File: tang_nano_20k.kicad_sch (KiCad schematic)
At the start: 11 parts, among them J3 Conn_Coaxial, J4 Conn_Coaxial, J5 Conn_01x02_Pin, J6 Conn_01x02_Pin, J7 Conn_01x04_Pin, U2 Tang_Nano_20K, U5 Adafruit_PCM510x

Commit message: Added information about DIN/RCA connectors
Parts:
- J5: footprint (none) -> Connector_PinHeader_2.54mm:PinHeader_1x02_P2.54mm_Vertical
- J6: footprint (none) -> Connector_PinHeader_2.54mm:PinHeader_1x02_P2.54mm_Vertical_SMD_Pin1Left
- J7: footprint (none) -> Connector_PinHeader_2.54mm:PinHeader_1x04_P2.54mm_Vertical
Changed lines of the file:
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@@
 			)
 		)
-		(property "Footprint" ""
+		(property "Footprint" "Connector_PinHeader_2.54mm:PinHeader_1x02_P2.54mm_Vertical_SMD_Pin1Left"
 			(at 210.82 101.6 0)
 			(hide yes)
@@
 			)
 		)
-		(property "Footprint" ""
+		(property "Footprint" "Connector_PinHeader_2.54mm:PinHeader_1x04_P2.54mm_Vertical"
 			(at 210.82 77.47 0)
 			(hide yes)
@@
 			)
 		)
-		(property "Datasheet" ""
+		(property "Datasheet" "https://www.kycon.com/Catalog_PDF/KLPX.pdf"
 			(at 68.58 115.57 0)
 			(hide yes)
@@
 			)
 		)
-		(property "Description" "coaxial connector (BNC, SMA, SMB, SMC, Cinch/RCA, LEMO, ...)"
+		(property "Description" "Kycon KLPX-0848A RCA card-edge female RCA connector"
 			(at 68.58 115.57 0)
 			(hide yes)
@@
 			)
 		)
-		(property "Footprint" ""
+		(property "Footprint" "Connector_PinHeader_2.54mm:PinHeader_1x02_P2.54mm_Vertical"
 			(at 210.82 91.44 0)
 			(hide yes)
@@
 			)
 		)
-		(property "Datasheet" ""
+		(property "Datasheet" "https://www.kycon.com/Catalog_PDF/KLPX.pdf"
 			(at 220.98 128.27 0)
 			(hide yes)
@@
 			)
 		)
-		(property "Description" "coaxial connector (BNC, SMA, SMB, SMC, Cinch/RCA, LEMO, ...)"
+		(property "Description" "Kycon KLPX-0848A RCA card-edge female RCA connector"
 			(at 220.98 128.27 0)
 			(hide yes)

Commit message: New official footprints for DIN/RCA
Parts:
- J3, J4: footprint (none) -> noaidi-fpga-synth:RCA_Kycon_KLPX-0848A
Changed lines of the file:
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@@
 			)
 		)
-		(property "Footprint" ""
+		(property "Footprint" "noaidi-fpga-synth:RCA_Kycon_KLPX-0848A"
 			(at 68.58 115.57 0)
 			(hide yes)
@@
 			)
 		)
-		(property "Footprint" ""
+		(property "Footprint" "noaidi-fpga-synth:RCA_Kycon_KLPX-0848A"
 			(at 220.98 128.27 0)
 			(hide yes)

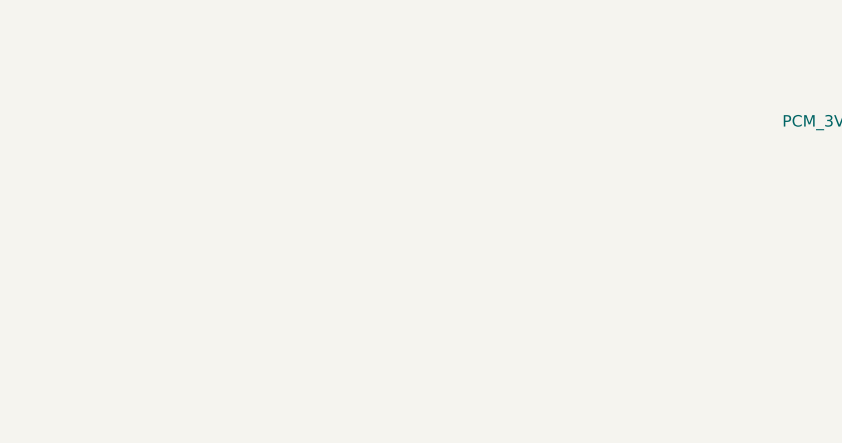
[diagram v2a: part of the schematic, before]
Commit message: Added LM66100 ideal diodes for power source switching.
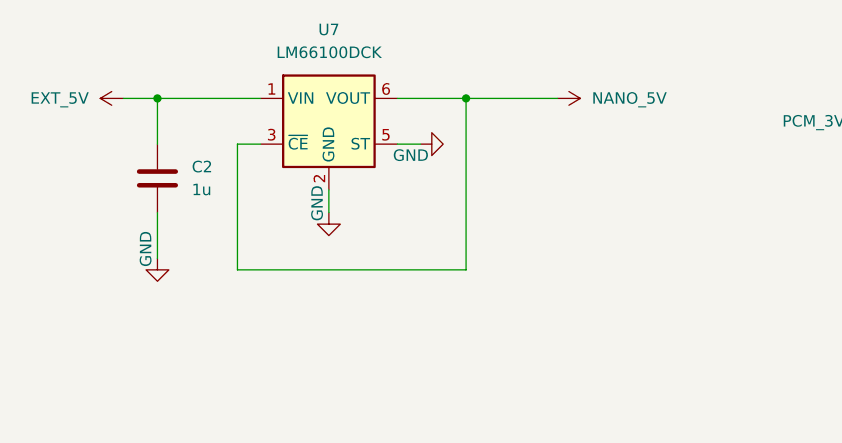
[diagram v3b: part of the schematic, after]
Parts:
- added C2: 1u, symbol Device:C
- added U7: LM66100DCK, Package_TO_SOT_SMD:SOT-363_SC-70-6, symbol Power_Management:LM66100DCK
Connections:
- net GND: now also C2.2, U7.2 (GND), U7.5 (ST)
- net NANO_5V: now also U7.3 (~{CE}), U7.6 (VOUT)
- new net EXT_5V: C2.1, U7.1 (VIN)
